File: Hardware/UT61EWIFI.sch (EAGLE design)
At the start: 18 parts, among them J1 ESPFLASH-2X3-1.27-SHROUDED, SW1 RESET

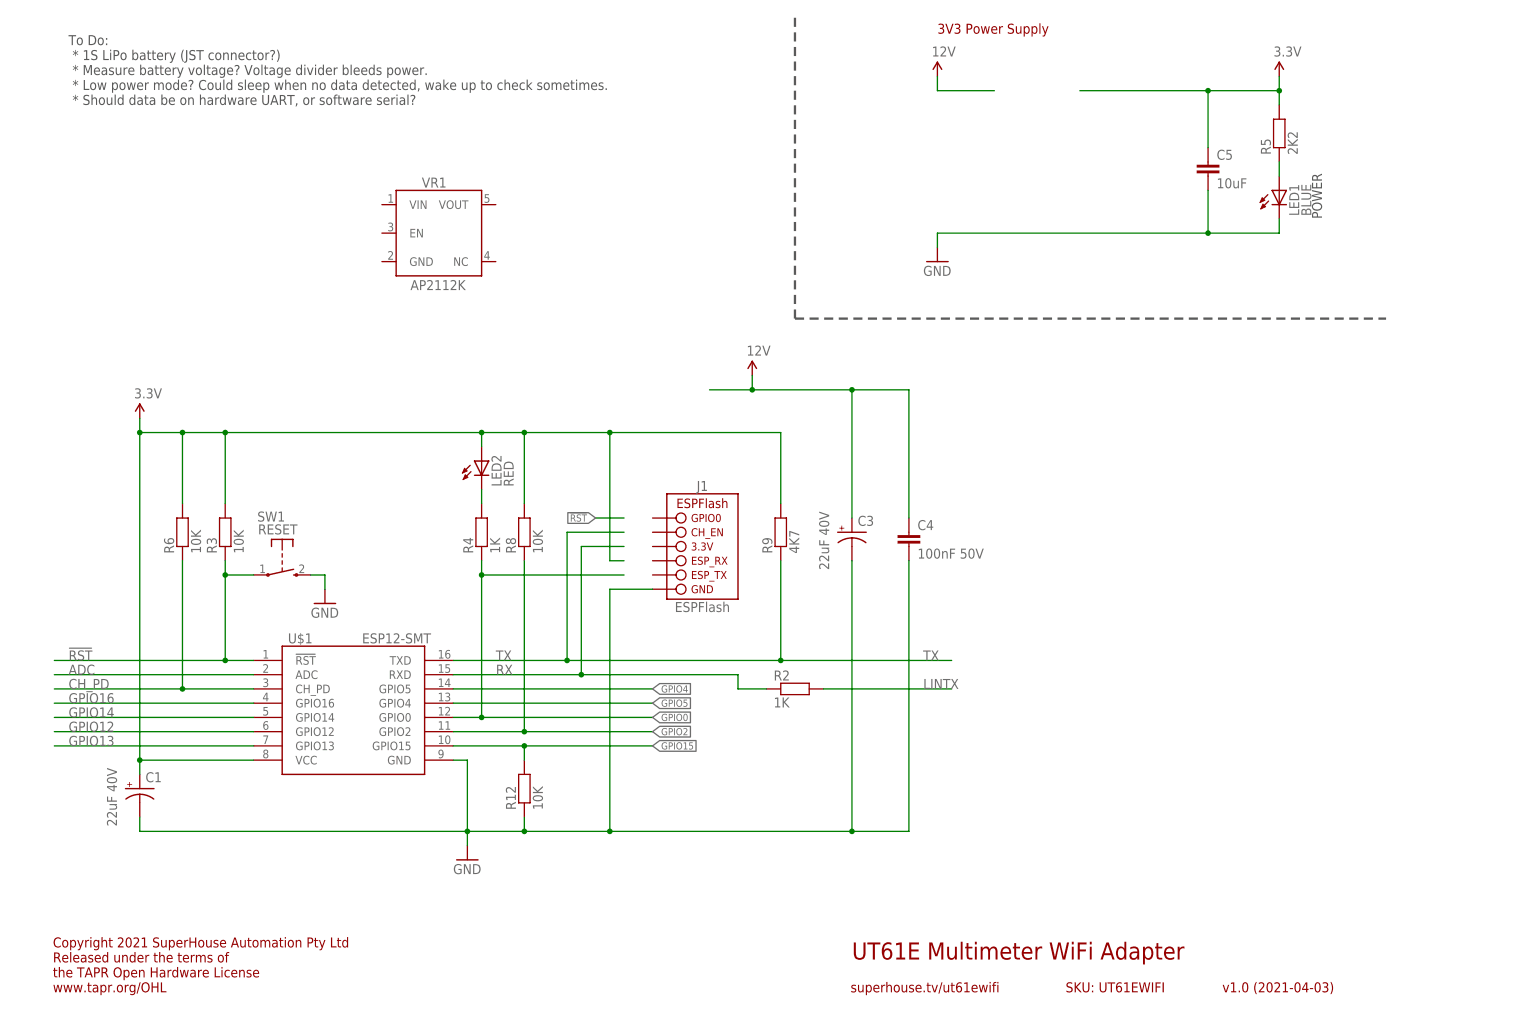
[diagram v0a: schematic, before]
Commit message: Added voltage regulator. Added IR input.
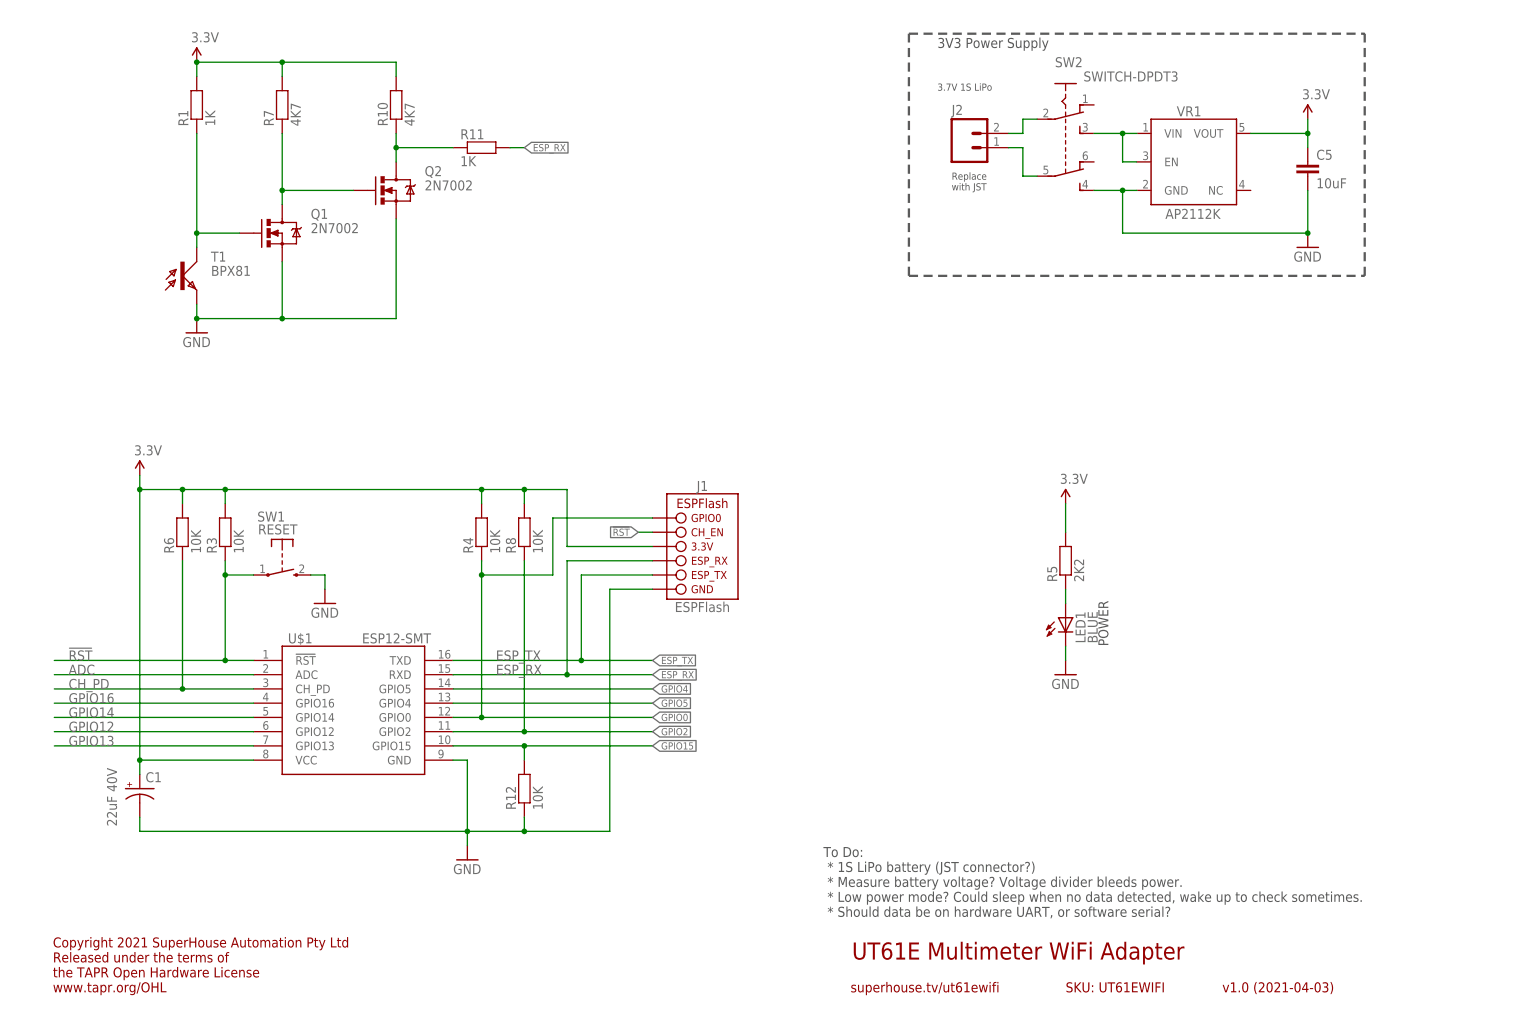
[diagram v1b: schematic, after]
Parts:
- removed C3: 22uF 40V, SuperHouse-DiscreteSemi:CAP_POLC
- removed C4: 100nF 50V, SuperHouse-DiscreteSemi:CAP0603
- removed LED2: RED, SuperHouse-LEDs:LED0603
- removed R2: 1K, SuperHouse-DiscreteSemi:RESISTOR0603
- removed R9: 4K7, SuperHouse-DiscreteSemi:RESISTOR0603
- added J2: (no value), SuperHouse-Connectors:M02-PLAIN
- added Q1, Q2: 2N7002, SuperHouse-DiscreteSemi:MOSFET-NCHANNEL-233
- added R1, R11: 1K, SuperHouse-DiscreteSemi:RESISTOR0603
- added R10, R7: 4K7, SuperHouse-DiscreteSemi:RESISTOR0603
- added SW2: SWITCH-DPDT3, SuperHouse-Switches:SWITCH-DPDT3
- added T1: BPX81, SuperHouse-Sensors:BPX81
- R4: value 1K -> 10K
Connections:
- removed net 12V: C3.+, C4.1
- removed net LINTX: R2.2
- removed net N$20: LED2.C, R4.2
- removed net RX: R2.1, U$1.RXD
- removed net TX: R9.1, U$1.TXD
- new net ESP_RX: J1.ESP_RX, R11.2, U$1.RXD
- new net ESP_TX: J1.ESP_TX, U$1.TXD
- new net N$1: Q2.D, R10.1, R11.1
- new net N$3: Q1.D, Q2.G, R7.1
- new net N$4: J2.2, SW2.2
- new net N$5: Q1.G, R1.1, T1.C
- new net N$6: SW2.3, VR1.EN, VR1.VIN
- new net N$7: J2.1, SW2.5
- net !RST: now also J1.CH_EN
- net 3.3V: now also J1.3.3V, R1.2, R10.2, R4.2, R7.2, VR1.VOUT; no longer LED2.A, R9.2
- net GND: now also Q1.S, Q2.S, SW2.4, T1.E, VR1.GND; no longer C3.-, C4.2
- net GPIO0: now also J1.GPIO0
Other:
- note added: "3.7V 1S LiPo"
- note added: "Replace with JST"
- moved on the sheet: C5, LED1, R5, VR1

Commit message: Changed multimeter data pin from D0 to D5 for v1.1 release.
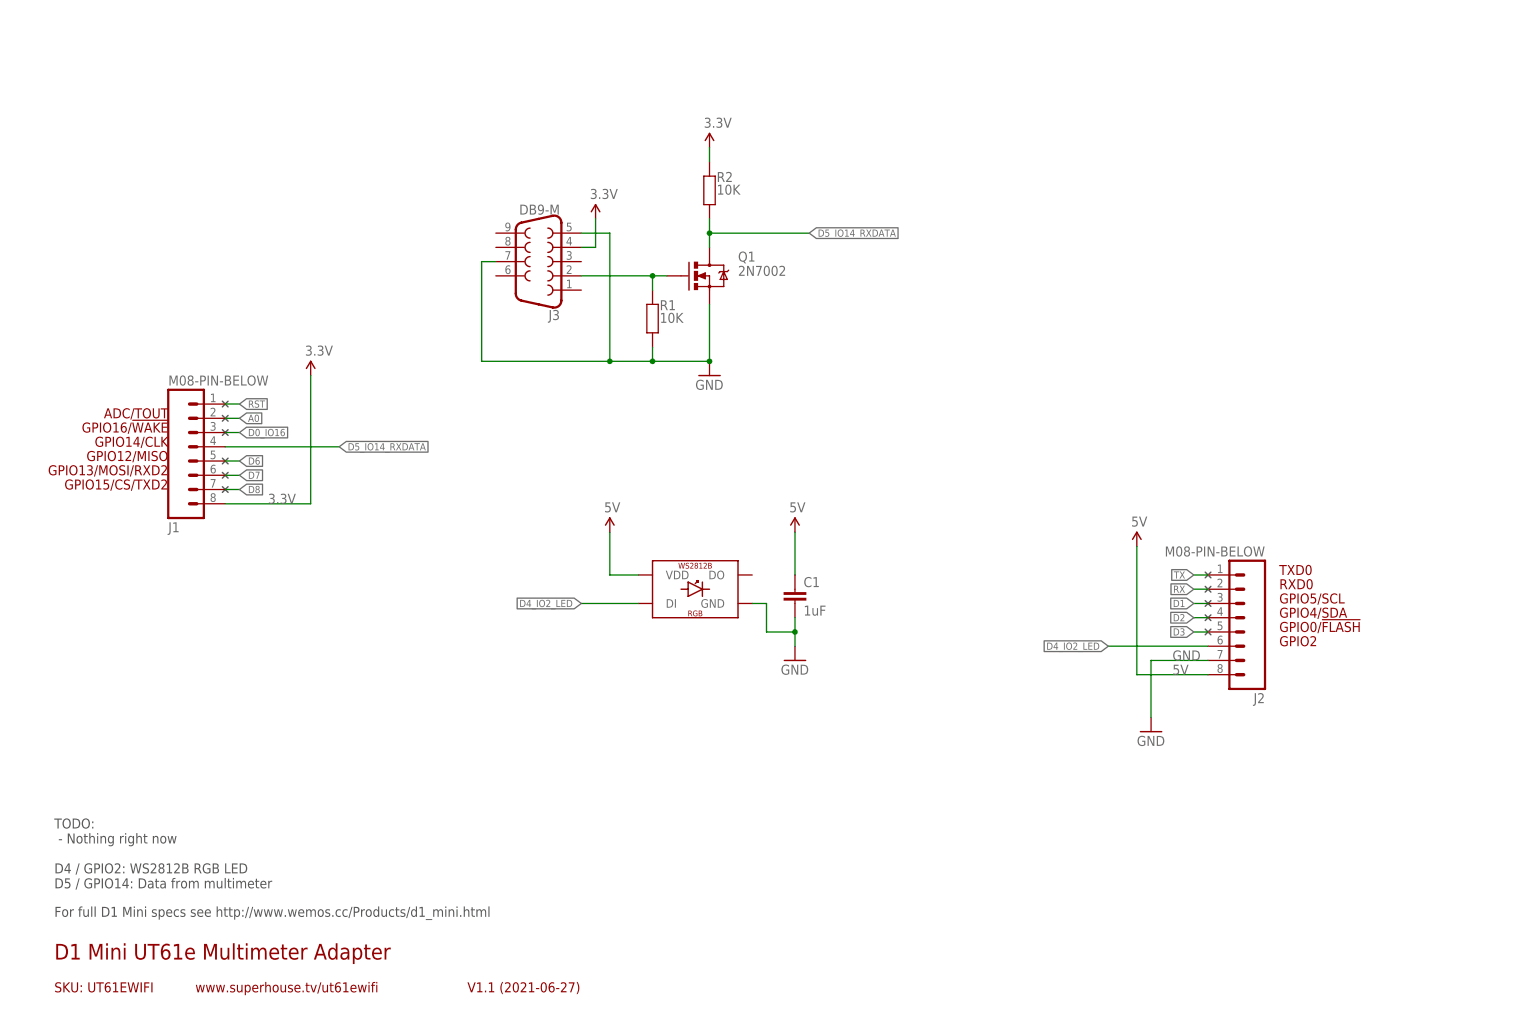
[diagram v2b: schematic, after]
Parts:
- removed C5: 10uF, SuperHouse-DiscreteSemi:CAP0805
- removed Q2: 2N7002, SuperHouse-DiscreteSemi:MOSFET-NCHANNEL-233
- removed R10, R7: 4K7, SuperHouse-DiscreteSemi:RESISTOR0603
- removed R11: 1K, SuperHouse-DiscreteSemi:RESISTOR0603
- removed R12, R3, R4, R6, R8: 10K, SuperHouse-DiscreteSemi:RESISTOR0603
- removed R5: 2K2, SuperHouse-DiscreteSemi:RESISTOR0603
- removed SW1: RESET, SuperHouse-Switches:TAC_SWITCH_2PINSMT
- removed SW2: SWITCH-DPDT3, SuperHouse-Switches:SWITCH-DPDT3
- removed T1: BPX81, SuperHouse-Sensors:BPX81
- removed U$1: ESP12-SMT, SuperHouse-MCUs:ESP12-SMT
- removed VR1: AP2112KSOT25, SuperHouse-Regulators:AP2112KSOT25
- added J3: DB9-M, SuperHouse-Connectors:DB9-PCB-PLUG
- added R2: 10K, SuperHouse-Resistors:RESISTOR0603
- C1: value 22uF 40V -> 1uF; device SuperHouse-DiscreteSemi:CAP_POLC -> SuperHouse-Capacitors:CAP0603
- J1: value ESPFLASH-2X3-1.27-SHROUDED -> M08-PIN-BELOW; device SuperHouse-ESPFlash:ESPFLASH-2X3-1.27-SHROUDED -> SuperHouse-Connectors:M08-PIN-BELOW
- J2: value (none) -> M08-PIN-BELOW; device SuperHouse-Connectors:M02-PLAIN -> SuperHouse-Connectors:M08-PIN-BELOW
- LED1: value BLUE -> WS2812B; device SuperHouse-LEDs:LED0603 -> SuperHouse-LEDs:WS2812B5050
- Q1: device SuperHouse-DiscreteSemi:MOSFET-NCHANNEL-233 -> SuperHouse-Transistors:MOSFET-NCHANNEL-233
- R1: value 1K -> 10K; device SuperHouse-DiscreteSemi:RESISTOR0603 -> SuperHouse-Resistors:RESISTOR0603
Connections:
- removed net !RST: J1.CH_EN, R3.1, SW1.P, U$1.!RST
- removed net ADC: U$1.ADC
- removed net CH_PD: R6.1, U$1.CH_PD
- removed net ESP_RX: J1.ESP_RX, R11.2, U$1.RXD
- removed net ESP_TX: J1.ESP_TX, U$1.TXD
- removed net GPIO0: J1.GPIO0, R4.1, U$1.GPIO0
- removed net GPIO12: U$1.GPIO12
- removed net GPIO13: U$1.GPIO13
- removed net GPIO14: U$1.GPIO14
- removed net GPIO15: R12.2, U$1.GPIO15
- removed net GPIO16: U$1.GPIO16
- removed net GPIO2: R8.1, U$1.GPIO2
- removed net GPIO4: U$1.GPIO5
- removed net GPIO5: U$1.GPIO4
- removed net N$14: LED1.A, R5.1
- removed net N$3: Q1.D, Q2.G, R7.1
- removed net N$4: J2.2, SW2.2
- removed net N$5: Q1.G, R1.1, T1.C
- removed net N$6: SW2.3, VR1.EN, VR1.VIN
- removed net N$7: J2.1, SW2.5
- new net 5V: C1.1, J2.8, LED1.VDD
- new net A0: J1.2
- new net D0_IO16: J1.3
- new net D1: J2.3
- new net D2: J2.4
- new net D3: J2.5
- new net D4_IO2_LED: J2.6, LED1.DI
- new net D5_IO14_RXDATA: J1.4, Q1.D, R2.1
- new net D6: J1.5
- new net D7: J1.6
- new net D8: J1.7
- new net RST: J1.1
- new net RX: J2.2
- new net TX: J2.1
- net 3.3V: now also J1.8, J3.4, R2.2; no longer C1.+, C5.1, J1.3.3V, R1.2, R10.2, R3.2, R4.2, R5.2, R6.2, R7.2, R8.2, U$1.VCC, VR1.VOUT
- net GND: now also C1.2, J2.7, J3.5, J3.7, LED1.GND, R1.1; no longer C1.-, C5.2, J1.GND, LED1.C, Q2.S, R12.1, SW1.S, SW2.4, T1.E, U$1.GND, VR1.GND
- net N$1: now also J3.2, Q1.G, R1.2; no longer Q2.D, R10.1, R11.1
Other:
- note added: "ADC/TOUT"
- note added: "D1 Mini UT61e Multimeter Adapter"
- note added: "For full D1 Mini specs see http://www.wemos.cc/Products/d1_mini.html"
- note added: "GPIO0/!FLASH"
- note added: "GPIO12/MISO"
- note added: "GPIO13/MOSI/RXD2"
- note added: "GPIO14/CLK"
- note added: "GPIO15/CS/TXD2"
- note added: "GPIO16/!WAKE"
- note added: "GPIO2"
- note added: "GPIO4/SDA"
- note added: "GPIO5/SCL"
- note added: "RXD0"
- note added: "TODO: - Nothing right now D4 / GPIO2: WS2812B RGB LED D5 / GPIO14: Data from multimeter"
- note added: "TXD0"
- note added: "V1.1 (2021-06-27)"
- note added: "www.superhouse.tv/ut61ewifi"
- note removed: "3.7V 1S LiPo"
- note removed: "3V3 Power Supply"
- note removed: "Copyright 2021 SuperHouse Automation Pty Ltd Released under the terms of the TAPR Open Hardware License www.tapr.org/OHL"
- note removed: "POWER"
- note removed: "Replace with JST"
- note removed: "To Do: * 1S LiPo battery (JST connector?) * Measure battery voltage? Voltage divider bleeds power. * Low power mode? Could sleep when no data detected, wake up to check sometimes. * Should data be on hardware UART, or software serial?"
- note removed: "UT61E Multimeter WiFi Adapter"
- note removed: "superhouse.tv/ut61ewifi"
- note removed: "v1.0 (2021-04-03)"
- moved on the sheet: Q1, R1
